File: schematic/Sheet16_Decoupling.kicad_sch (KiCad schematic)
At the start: 11 parts

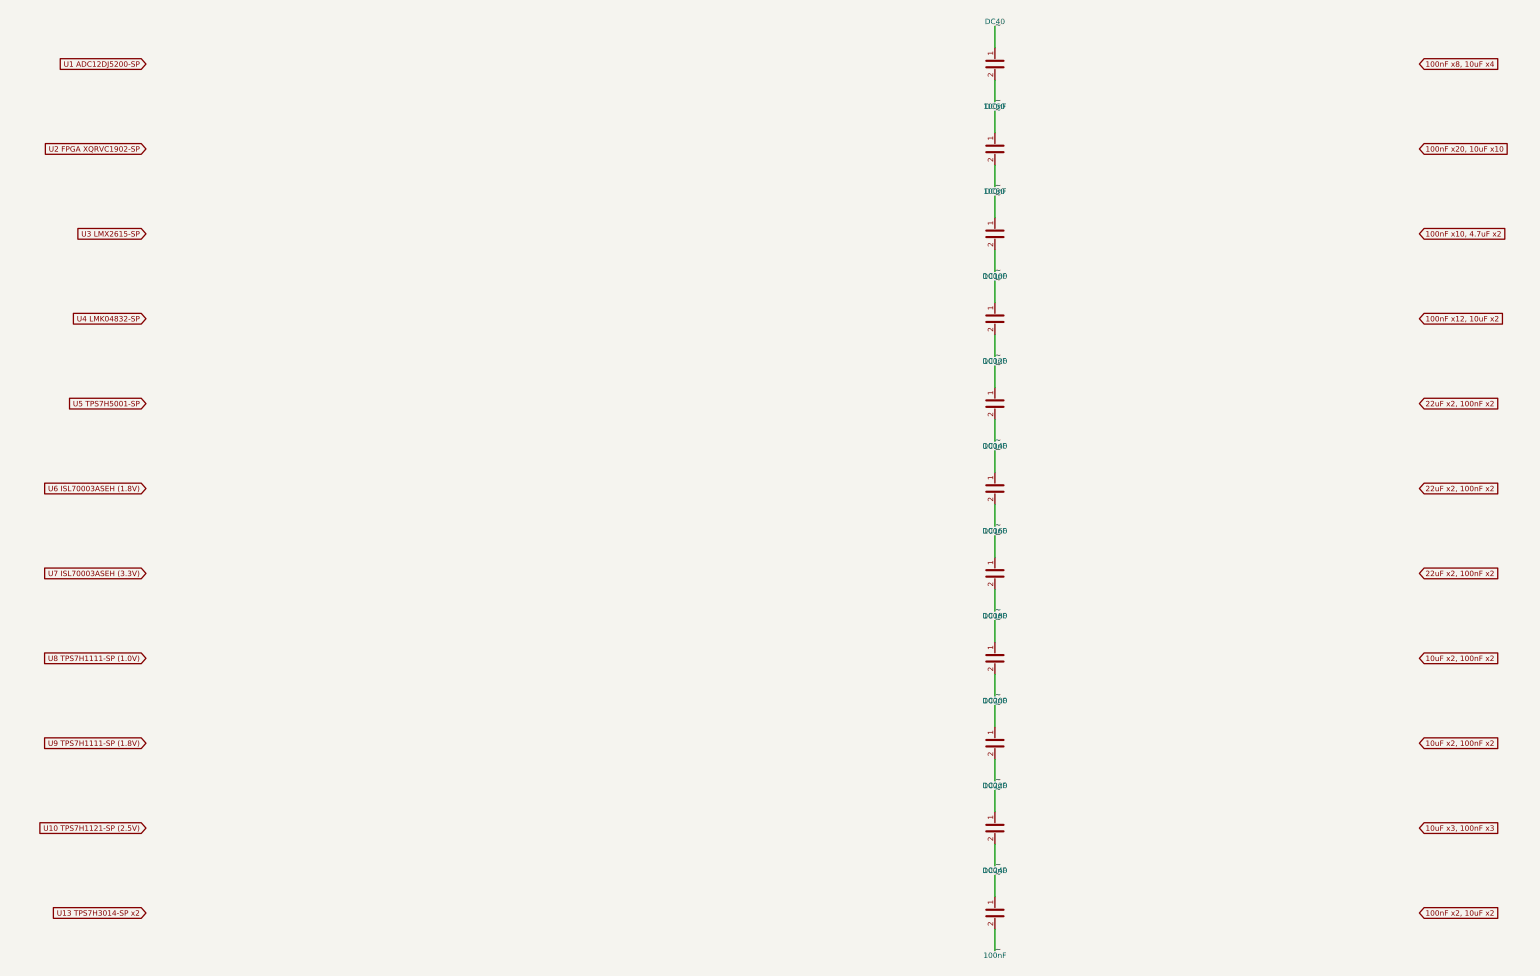
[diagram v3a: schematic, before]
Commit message: Fix KiCad schematic wiring: Y-inversion bug + all 891 pins connected
- Fixed critical Y-axis inversion bug: KiCad inverts Y when placing
  symbols (lib Y + schematic Y = abs Y is WRONG; correct: abs Y = sym Y - lib Y)
- This caused ALL wires to connect to wrong pins (e.g., CS label connected
  to BG pin instead of CS pin)
- Verified with netlist: 0 unconnected nets, all pin functions correct
- Fixed wire direction for angle 90/270 (swapped due to Y-inversion)
- 891 pin connections across 15 sheets, all 17 sheets export without errors
- Netlist verification: CS→E8, BG→C3, INA+→A4, CLK+→F1, JESD pairs correct

Co-Authored-By: opencode <noreply@opencode.ai>
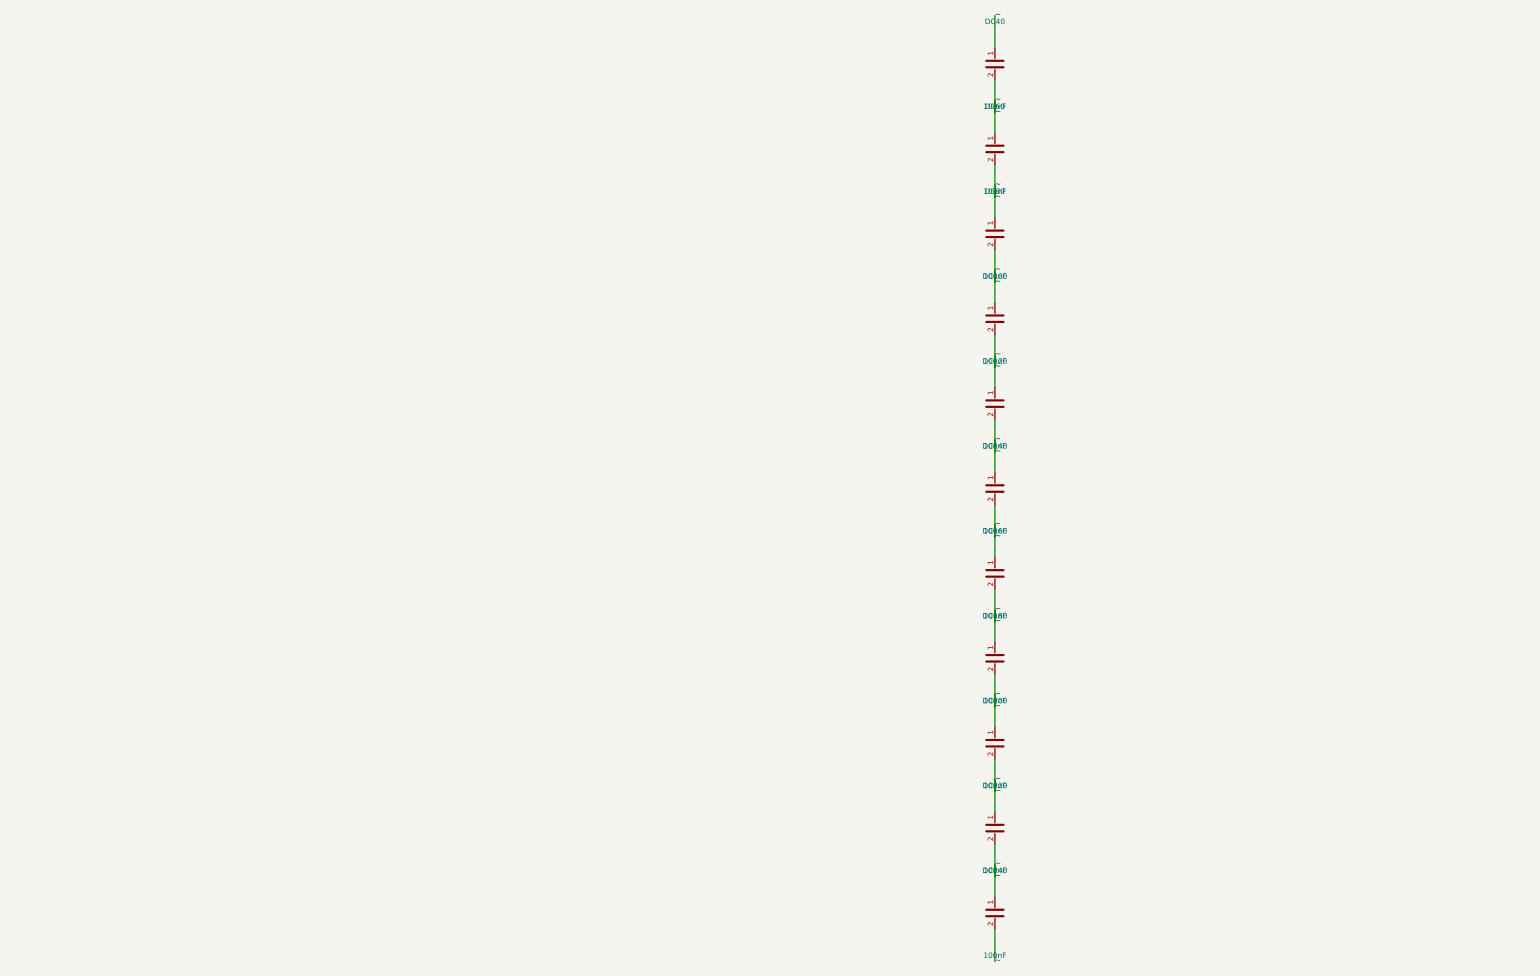
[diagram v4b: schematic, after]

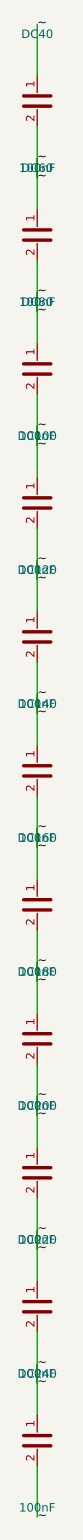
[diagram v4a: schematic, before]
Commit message: fix: isolate ISL70003ASEH buck pins, fix LMX_SYNC collision, NC pins, connector pin names
- ISL70003ASEH pins now use ref prefix (U6_LX1 vs U7_LX1) to prevent shorts
- Buck SYNC pins separated from LMX_SYNC (power sync ≠ PLL sync)
- NC pins properly skipped (unconnected)
- Connector PIN_1..PIN_6 use ref prefix (J1_PIN_1 vs J2_PIN_1)
- Fixed annotation warnings in Sheet13 (C_dev→C125, R_dev→R74, U_TPS7H→U14)
- Regenerated all PDFs and SVGs
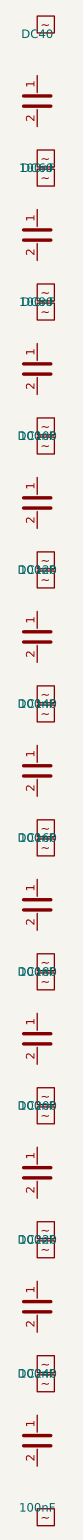
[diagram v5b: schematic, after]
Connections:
- net ~: no longer DC100.1, DC100.2, DC120.1, DC120.2, DC140.1, DC140.2, DC160.1, DC160.2, DC180.1, DC180.2, DC200.1, DC200.2, DC220.1, DC220.2, DC240.1, DC240.2, DC40.1, DC40.2, DC60.1, DC60.2, DC80.1, DC80.2
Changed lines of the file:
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@@
     (pin "2")
   )
-  (wire (pts (xy 280.0000 36.1900) (xy 280.0000 28.5700)) (stroke (width 0) (type default)))
-  (label "~" (at 280.0000 28.5700 0) (effects (font (size 1.27 1.27))))
-  (wire (pts (xy 280.0000 43.8100) (xy 280.0000 51.4300)) (stroke (width 0) (type default)))
-  (label "~" (at 280.0000 51.4300 0) (effects (font (size 1.27 1.27))))
-  (wire (pts (xy 280.0000 56.1900) (xy 280.0000 48.5700)) (stroke (width 0) (type default)))
-  (label "~" (at 280.0000 48.5700 0) (effects (font (size 1.27 1.27))))
-  (wire (pts (xy 280.0000 63.8100) (xy 280.0000 71.4300)) (stroke (width 0) (type default)))
-  (label "~" (at 280.0000 71.4300 0) (effects (font (size 1.27 1.27))))
-  (wire (pts (xy 280.0000 76.1900) (xy 280.0000 68.5700)) (stroke (width 0) (type default)))
-  (label "~" (at 280.0000 68.5700 0) (effects (font (size 1.27 1.27))))
-  (wire (pts (xy 280.0000 83.8100) (xy 280.0000 91.4300)) (stroke (width 0) (type default)))
-  (label "~" (at 280.0000 91.4300 0) (effects (font (size 1.27 1.27))))
-  (wire (pts (xy 280.0000 96.1900) (xy 280.0000 88.5700)) (stroke (width 0) (type default)))
-  (label "~" (at 280.0000 88.5700 0) (effects (font (size 1.27 1.27))))
-  (wire (pts (xy 280.0000 103.8100) (xy 280.0000 111.4300)) (stroke (width 0) (type default)))
-  (label "~" (at 280.0000 111.4300 0) (effects (font (size 1.27 1.27))))
-  (wire (pts (xy 280.0000 116.1900) (xy 280.0000 108.5700)) (stroke (width 0) (type default)))
-  (label "~" (at 280.0000 108.5700 0) (effects (font (size 1.27 1.27))))
-  (wire (pts (xy 280.0000 123.8100) (xy 280.0000 131.4300)) (stroke (width 0) (type default)))
-  (label "~" (at 280.0000 131.4300 0) (effects (font (size 1.27 1.27))))
-  (wire (pts (xy 280.0000 136.1900) (xy 280.0000 128.5700)) (stroke (width 0) (type default)))
-  (label "~" (at 280.0000 128.5700 0) (effects (font (size 1.27 1.27))))
-  (wire (pts (xy 280.0000 143.8100) (xy 280.0000 151.4300)) (stroke (width 0) (type default)))
-  (label "~" (at 280.0000 151.4300 0) (effects (font (size 1.27 1.27))))
-  (wire (pts (xy 280.0000 156.1900) (xy 280.0000 148.5700)) (stroke (width 0) (type default)))
-  (label "~" (at 280.0000 148.5700 0) (effects (font (size 1.27 1.27))))
-  (wire (pts (xy 280.0000 163.8100) (xy 280.0000 171.4300)) (stroke (width 0) (type default)))
-  (label "~" (at 280.0000 171.4300 0) (effects (font (size 1.27 1.27))))
-  (wire (pts (xy 280.0000 176.1900) (xy 280.0000 168.5700)) (stroke (width 0) (type default)))
-  (label "~" (at 280.0000 168.5700 0) (effects (font (size 1.27 1.27))))
-  (wire (pts (xy 280.0000 183.8100) (xy 280.0000 191.4300)) (stroke (width 0) (type default)))
-  (label "~" (at 280.0000 191.4300 0) (effects (font (size 1.27 1.27))))
-  (wire (pts (xy 280.0000 196.1900) (xy 280.0000 188.5700)) (stroke (width 0) (type default)))
-  (label "~" (at 280.0000 188.5700 0) (effects (font (size 1.27 1.27))))
-  (wire (pts (xy 280.0000 203.8100) (xy 280.0000 211.4300)) (stroke (width 0) (type default)))
-  (label "~" (at 280.0000 211.4300 0) (effects (font (size 1.27 1.27))))
-  (wire (pts (xy 280.0000 216.1900) (xy 280.0000 208.5700)) (stroke (width 0) (type default)))
-  (label "~" (at 280.0000 208.5700 0) (effects (font (size 1.27 1.27))))
-  (wire (pts (xy 280.0000 223.8100) (xy 280.0000 231.4300)) (stroke (width 0) (type default)))
-  (label "~" (at 280.0000 231.4300 0) (effects (font (size 1.27 1.27))))
-  (wire (pts (xy 280.0000 236.1900) (xy 280.0000 228.5700)) (stroke (width 0) (type default)))
-  (label "~" (at 280.0000 228.5700 0) (effects (font (size 1.27 1.27))))
-  (wire (pts (xy 280.0000 243.8100) (xy 280.0000 251.4300)) (stroke (width 0) (type default)))
-  (label "~" (at 280.0000 251.4300 0) (effects (font (size 1.27 1.27))))
+  (global_label "~" (at 280.0000 28.5700 0) (effects (font (size 1.27 1.27))))
+  (global_label "~" (at 280.0000 51.4300 0) (effects (font (size 1.27 1.27))))
+  (global_label "~" (at 280.0000 48.5700 0) (effects (font (size 1.27 1.27))))
+  (global_label "~" (at 280.0000 71.4300 0) (effects (font (size 1.27 1.27))))
+  (global_label "~" (at 280.0000 68.5700 0) (effects (font (size 1.27 1.27))))
+  (global_label "~" (at 280.0000 91.4300 0) (effects (font (size 1.27 1.27))))
+  (global_label "~" (at 280.0000 88.5700 0) (effects (font (size 1.27 1.27))))
+  (global_label "~" (at 280.0000 111.4300 0) (effects (font (size 1.27 1.27))))
+  (global_label "~" (at 280.0000 108.5700 0) (effects (font (size 1.27 1.27))))
+  (global_label "~" (at 280.0000 131.4300 0) (effects (font (size 1.27 1.27))))
+  (global_label "~" (at 280.0000 128.5700 0) (effects (font (size 1.27 1.27))))
+  (global_label "~" (at 280.0000 151.4300 0) (effects (font (size 1.27 1.27))))
+  (global_label "~" (at 280.0000 148.5700 0) (effects (font (size 1.27 1.27))))
+  (global_label "~" (at 280.0000 171.4300 0) (effects (font (size 1.27 1.27))))
+  (global_label "~" (at 280.0000 168.5700 0) (effects (font (size 1.27 1.27))))
+  (global_label "~" (at 280.0000 191.4300 0) (effects (font (size 1.27 1.27))))
+  (global_label "~" (at 280.0000 188.5700 0) (effects (font (size 1.27 1.27))))
+  (global_label "~" (at 280.0000 211.4300 0) (effects (font (size 1.27 1.27))))
+  (global_label "~" (at 280.0000 208.5700 0) (effects (font (size 1.27 1.27))))
+  (global_label "~" (at 280.0000 231.4300 0) (effects (font (size 1.27 1.27))))
+  (global_label "~" (at 280.0000 228.5700 0) (effects (font (size 1.27 1.27))))
+  (global_label "~" (at 280.0000 251.4300 0) (effects (font (size 1.27 1.27))))
   (sheet_instances (path "/" (page "1")))
 )
